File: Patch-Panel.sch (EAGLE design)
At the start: 55 parts, among them J1 APPPP45_PCB_VERT, J10 APPPP45_PCB_VERT, J11 APPPP45_PCB_VERT, J12 APPPP45_PCB_VERT, J13 APPPP45_PCB_VERT, J14 APPPP45_PCB_VERT, J15 APPPP45_PCB_VERT, J16 APPPP45_PCB_VERT, J17 APPPP45_PCB_VERT, J18 APPPP45_PCB_VERT, J19 APPPP45_PCB_VERT, J2 APPPP45_PCB_VERT, J20 APPPP45_PCB_VERT, J21 APPPP45_PCB_VERT, J22 APPPP45_PCB_VERT, J23 APPPP45_PCB_VERT, J24 APPPP45_PCB_VERT, J25 APPPP45_PCB_VERT, J26 APPPP45_PCB_VERT, J27 APPPP45_PCB_VERT, J28 APPPP45_PCB_VERT, J29 APPPP45_PCB_VERT, J3 APPPP45_PCB_VERT, J30 APPPP45_PCB_VERT, J31 APPPP45_PCB_VERT, J32 APPPP45_PCB_VERT, J33 APPPP45_PCB_VERT, J34 APPPP45_PCB_VERT, J35 APPPP45_PCB_VERT, J36 APPPP45_PCB_VERT, J37 APPPP45_PCB_VERT, J38 APPPP45_PCB_VERT, J39 APPPP45_PCB_VERT, J4 APPPP45_PCB_VERT, J40 APPPP45_PCB_VERT, J41 APPPP45_PCB_VERT, J42 APPPP45_PCB_VERT, J43 APPPP45_PCB_VERT, J44 APPPP45_PCB_VERT, J45 APPPP45_PCB_VERT, J46 APPPP45_PCB_VERT, J47 APPPP45_PCB_VERT, J5 APPPP45_PCB_VERT, J6 APPPP45_PCB_VERT, J7 APPPP45_PCB_VERT, J8 APPPP45_PCB_VERT

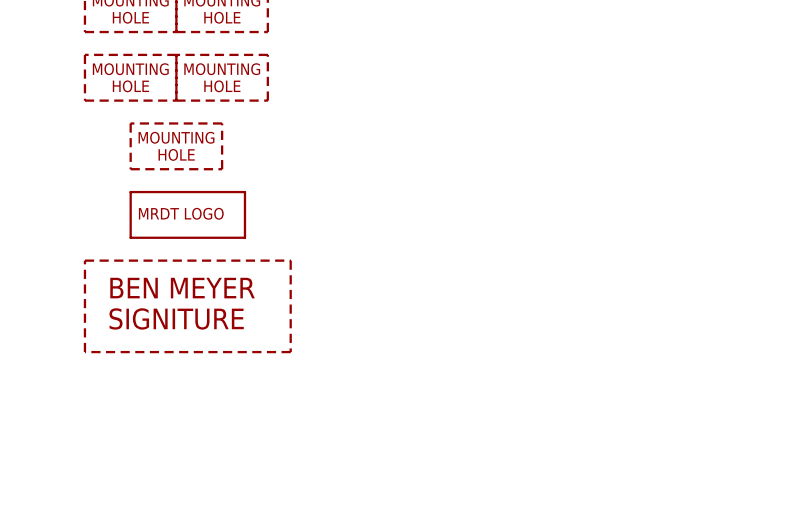
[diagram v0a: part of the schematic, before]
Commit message: Last edits before fabrication
tidied a couple traces and labels, and added a martian.
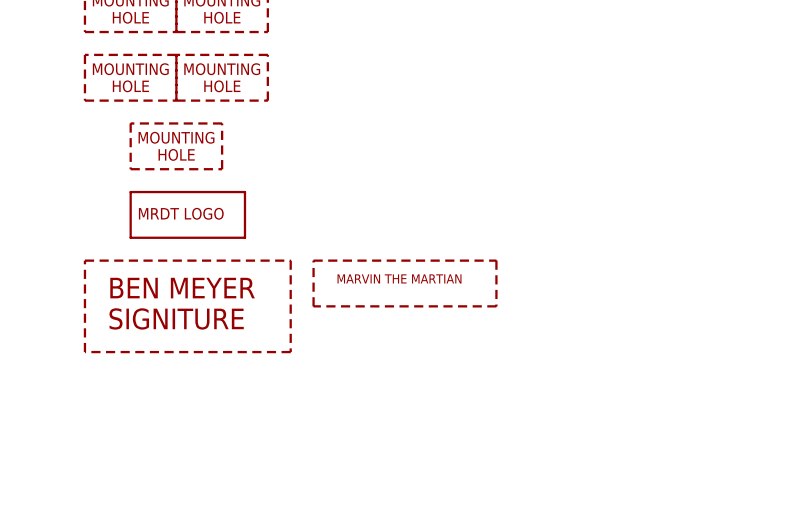
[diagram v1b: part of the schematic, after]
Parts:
- added U$2: MARVIN-THE-MARTIAN, MRDT-Hardware:MARVIN-THE-MARTIAN
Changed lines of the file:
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@@
 <?xml version="1.0" encoding="utf-8"?>
 <!DOCTYPE eagle SYSTEM "eagle.dtd">
-<eagle version="7.4.0">
+<eagle version="6.5.0">
 <drawing>
 <settings>
@@
 <part name="LOGO1" library="MRDT-Hardware" deviceset="MRDT_LOGO" device=""/>
 <part name="U$1" library="sig" deviceset="BEN-MEYER" device=""/>
+<part name="U$2" library="MRDT-Hardware" deviceset="MARVIN-THE-MARTIAN" device=""/>
 </parts>
 <sheets>
@@
 <instance part="LOGO1" gate="G$1" x="177.8" y="-134.62"/>
 <instance part="U$1" gate="G$1" x="172.72" y="-137.16"/>
+<instance part="U$2" gate="G$1" x="198.12" y="-142.24"/>
 </instances>
 <busses>

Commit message: 2018 Patch Panel Rev1
The 12V buses are being passed to patch panel. In order from bottom of power board to top, Actuation 15A, Logic 5A, Communication 5A.  There is no extra bus this year. Add one more Logic/Act connection
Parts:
- removed H1, H2: MOUNTING_HOLE#6, MRDT-Hardware:MOUNTING_HOLE#6
- removed J44, J45, J46, J47: APPPP45_PCB_VERT, MRDT-Connectors:APPPP45_PCB_VERT
- added J9: APPPP45_PCB_VERT, MRDT-Connectors:APPPP45_PCB_VERT
- U$1: value BEN-MEYER -> CONNIE_WENTWORTH_SIGNATURE; device sig:BEN-MEYER -> MRDT-Signatures:CONNIE_WENTWORTH_SIGNATURE
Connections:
- removed net EXT-12V: J44.P$1, J46.P$1, J7.P$1
- net ACT-12V: now also J9.P$1
- net COM-12V: now also J28.P$1, J30.P$1, J32.P$1, J34.P$1; no longer J36.P$1, J38.P$1, J40.P$1, J42.P$1
- net GND: now also J7.P$1; no longer J45.P$1, J47.P$1, J8.P$1
- net LOG-12V: now also J36.P$1, J38.P$1, J40.P$1, J42.P$1, J8.P$1; no longer J28.P$1, J30.P$1, J32.P$1, J34.P$1
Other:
- moved on the sheet: J2, J6, J7, J8
